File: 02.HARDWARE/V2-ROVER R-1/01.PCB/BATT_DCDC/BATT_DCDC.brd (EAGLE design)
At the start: 20.4 x 34.4 mm, 61 parts, among them J1 DF40C-20DP-0.4V_51_, K1 FLEX11, Q1 NVTFS9D6P04M8LTAG, Q2 2N7002PW, Q5 2N7002PW, U1 MCP6071T-E/OT, U3 TPS55330RTET, U7 MCP6071T-E/OT

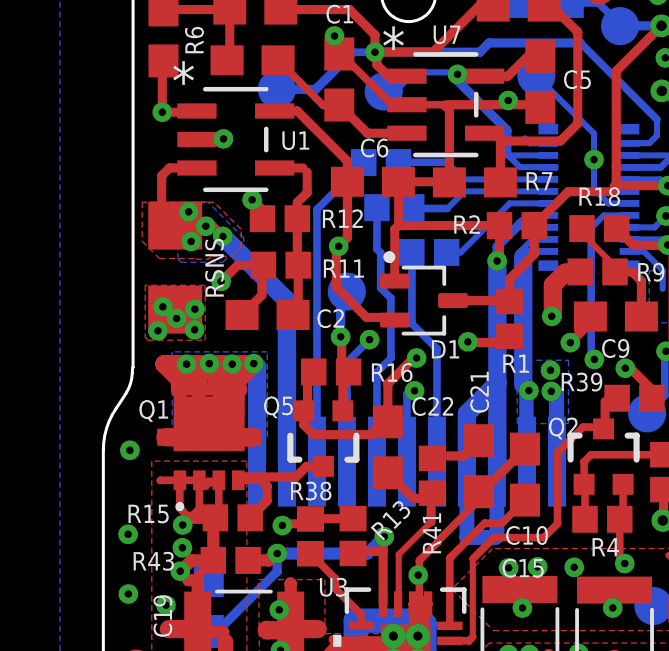
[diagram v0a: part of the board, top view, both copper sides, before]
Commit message: Separacion de las vias de la zona de cobre descubierto en la resistencia de sensado
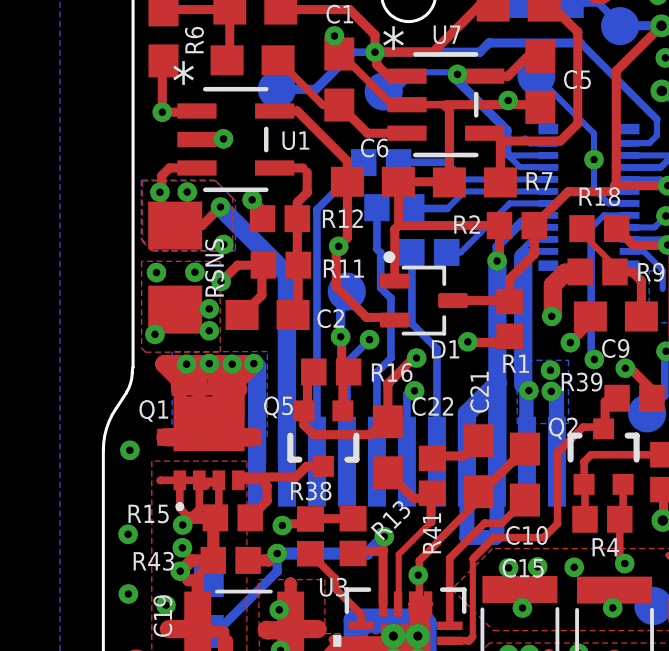
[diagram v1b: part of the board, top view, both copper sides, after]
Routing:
- net ISENSE_RAW: track 13.7 -> 16.4 mm
- net VOUT-: track 13.3 -> 14.3 mm

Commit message: Cierra el issue #65
Algunos cambios menores de rutado
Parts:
- moved R9 0.33 mm to (73.7, 25.9)
- moved R2 0.07 mm to (71.3, 27.4)
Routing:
- net VBUS: track 56.4 -> 64.9 mm
- net N$12: track 4.09 -> 4.95 mm
- net GND: vias 45 -> 46
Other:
- board text added: "BATT_DCDC ROVER R-1 v3-MAY'23"
- board text removed: "BATT_DCDC ROVER1K v2-DEC'22"

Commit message: Issue #72
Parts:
- removed Q5: 2N7002PW, SparkFun-DiscreteSemi:SOT323
- removed R15: 100k, SparkFun-Resistors:0402
- added U2: LM5114BMF_NOPB, LM5114BMF_NOPB:SOT95P280X145-6N
- R16: value 100k -> 10k
- moved C22 3.39 mm to (69.7, 22.0), turned to 180 degrees
- moved R16 0.78 mm to (65.9, 22.7), turned to 0 degrees
- moved C21 0.29 mm to (70.2, 19.2), turned to 270 degrees
- moved R41 0.29 mm to (68.8, 19.0), turned to 270 degrees
- moved C10 0.26 mm to (71.8, 19.1)
- moved R13 0.16 mm to (65.8, 16.9)
- moved R38 0.13 mm to (64.4, 16.9)
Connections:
- removed net N$8: Q1.4, Q5.3, R15.1
- new net N$9: Q1.4, U2.2, U2.3
- net GND: now also U2.4; no longer Q5.2
- net OP_SWITCH: now also U2.5; no longer Q5.1
- net VSOURCE: now also U2.1; no longer R15.2
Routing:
- net N$9: track 0.00 -> 5.95 mm
- net N$8: track 5.44 -> 0.00 mm
- net VSOURCE: track 34.7 -> 37.4 mm
- net COMP_TPS: track 6.07 -> 8.37 mm
- net SW2_TPS: track 29.6 -> 28.0 mm
- net VBUS: track 64.9 -> 63.5 mm
- net GND: track 141.2 -> 140.0 mm, vias 46 -> 47
- net OP_SWITCH: track 28.8 -> 28.1 mm
- net N$35: track 5.56 -> 6.13 mm
- net VOUT+: track 32.5 -> 33.0 mm
- net N$2: track 9.35 -> 9.85 mm

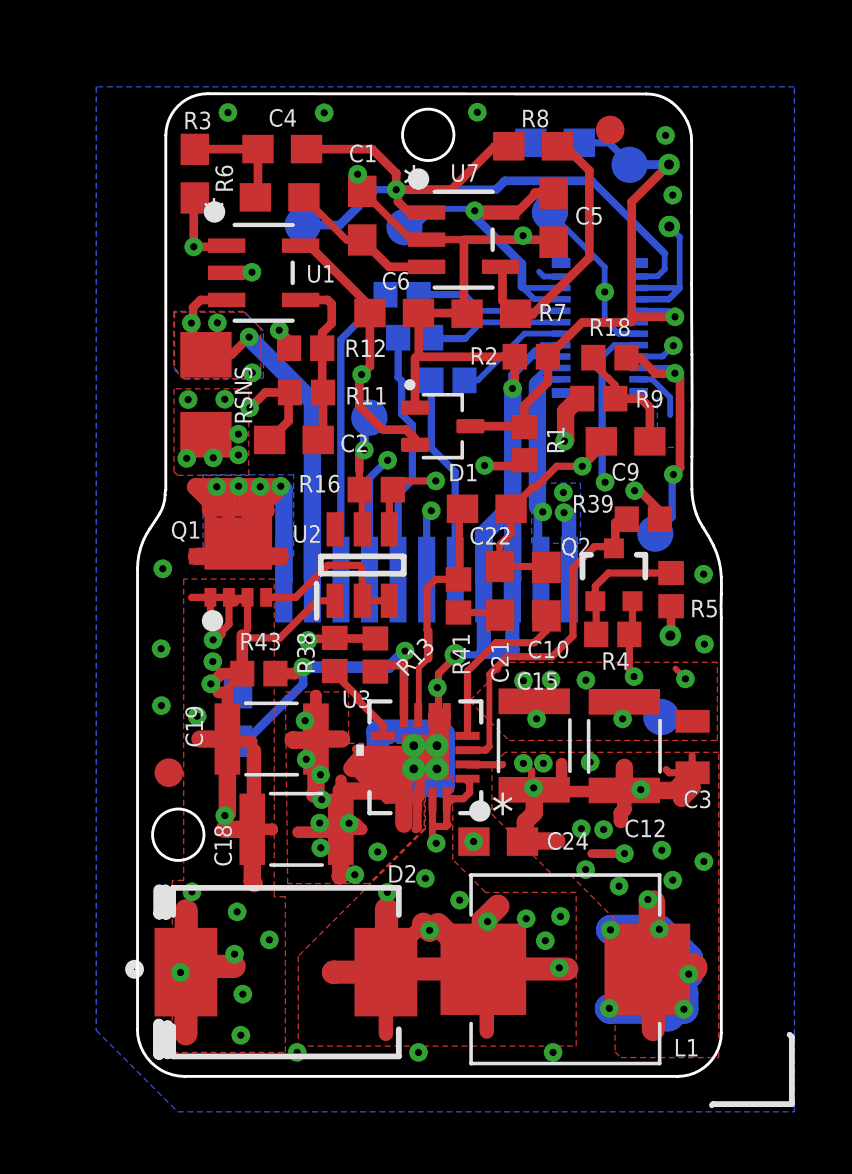
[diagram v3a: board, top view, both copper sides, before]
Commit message: Se corrige señal IN a VSOURCE para  que funcione como negador
Se mueven algunos componentes para  que no se solapen.
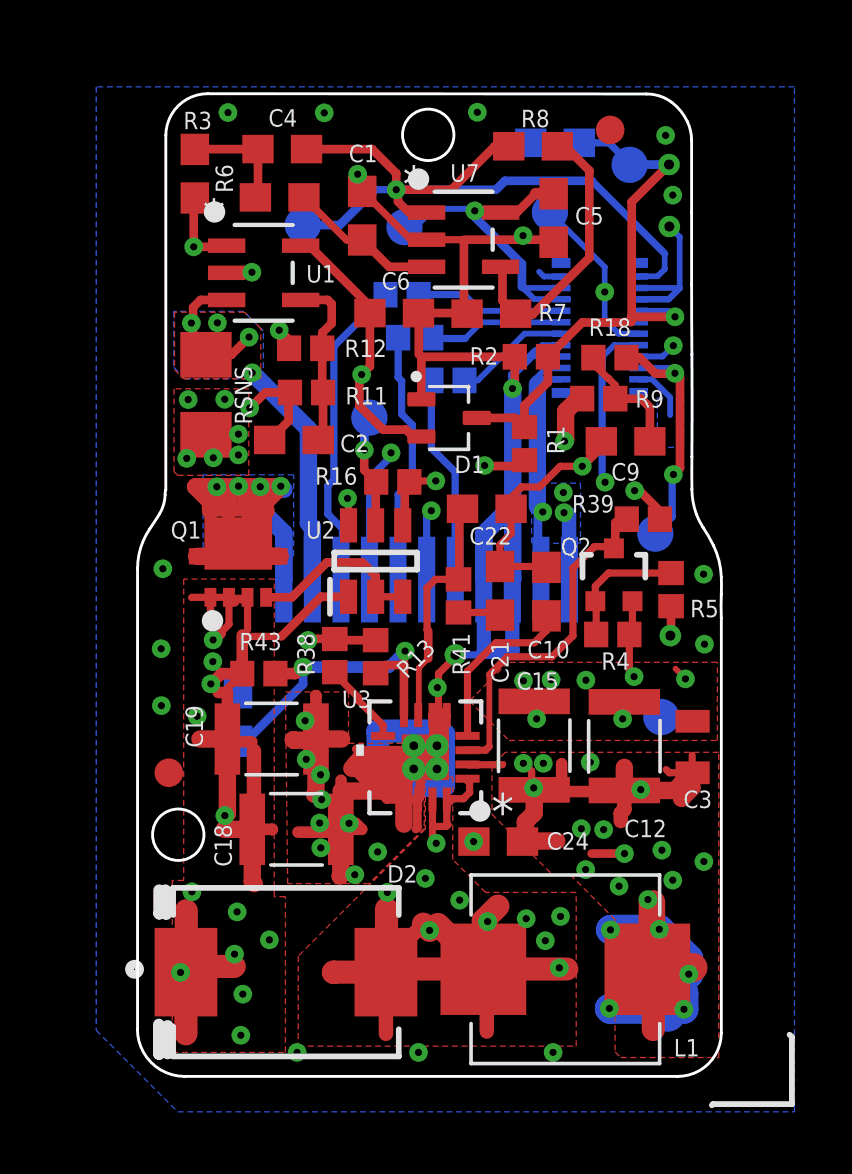
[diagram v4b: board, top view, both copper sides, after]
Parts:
- moved R16 0.64 mm to (66.5, 23.0)
- moved U2 0.49 mm to (65.8, 20.2)
- moved D1 0.36 mm to (68.4, 25.2)
- moved R13 0.06 mm to (65.8, 16.9)
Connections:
- net VSOURCE: now also U2.6
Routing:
- net VSOURCE: track 37.4 -> 45.8 mm, vias 12 -> 13
- net VOUT-: track 14.3 -> 13.1 mm
- net GND: track 140.0 -> 139.3 mm
- net VCC: track 49.0 -> 48.5 mm
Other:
- board text added: "BATT_DCDC ROVER R-1 v4-SEP'23"
- board text removed: "BATT_DCDC ROVER R-1 v3-MAY'23"

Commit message: Revision antes de envio SETI 3ra produccion - SEP-23
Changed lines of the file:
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@@
 <drawing>
 <settings>
-<setting alwaysvectorfont="no"/>
+<setting alwaysvectorfont="yes"/>
 <setting keepoldvectorfont="yes"/>
 <setting verticaltext="up"/>
@@
 <layer number="14" name="Route14" color="1" fill="6" visible="no" active="no"/>
 <layer number="15" name="Route15" color="13" fill="1" visible="no" active="yes"/>
-<layer number="16" name="Bottom" color="1" fill="1" visible="no" active="yes"/>
+<layer number="16" name="Bottom" color="1" fill="1" visible="yes" active="yes"/>
 <layer number="17" name="Pads" color="2" fill="1" visible="yes" active="yes"/>
 <layer number="18" name="Vias" color="2" fill="1" visible="yes" active="yes"/>
 <layer number="19" name="Unrouted" color="6" fill="1" visible="yes" active="yes"/>
 <layer number="20" name="Dimension" color="15" fill="1" visible="yes" active="yes"/>
-<layer number="21" name="tPlace" color="14" fill="1" visible="no" active="yes"/>
+<layer number="21" name="tPlace" color="14" fill="1" visible="yes" active="yes"/>
 <layer number="22" name="bPlace" color="13" fill="1" visible="yes" active="yes"/>
 <layer number="23" name="tOrigins" color="14" fill="1" visible="no" active="yes"/>
 <layer number="24" name="bOrigins" color="13" fill="1" visible="yes" active="yes"/>
-<layer number="25" name="tNames" color="7" fill="1" visible="no" active="yes"/>
+<layer number="25" name="tNames" color="7" fill="1" visible="yes" active="yes"/>
 <layer number="26" name="bNames" color="7" fill="1" visible="yes" active="yes"/>
 <layer number="27" name="tValues" color="7" fill="1" visible="no" active="yes"/>
@@
 <circle x="67.35" y="33.57" radius="0.17204375" width="0.4064" layer="21"/>
 <rectangle x1="59.8" y1="21.36" x2="62.28" y2="22.62" layer="29"/>
+<circle x="63.76" y="18.94" radius="0.17204375" width="0.4064" layer="21"/>
 </plain>
 <attributes>
@@
 </element>
 <element name="Q2" library="SparkFun-DiscreteSemi" package="SOT323" value="2N7002PW" x="74.19" y="19.72" smashed="yes">
-<attribute name="NAME" x="72.8645" y="20.708" size="0.6096" layer="25" font="vector" align="center"/>
+<attribute name="NAME" x="72.9345" y="21.028" size="0.6096" layer="25" font="vector" align="center"/>
 <attribute name="PROD_ID" value="TRANS-11151" x="1.11" y="5.46" size="1.778" layer="27" display="off"/>
 </element>
@@
 </element>
 <element name="R1" library="SparkFun-Resistors" library_urn="urn:adsk.eagle:library:532" package="0402" package3d_urn="urn:adsk.eagle:package:39657/1" value="169k" x="71.06" y="24.31" smashed="yes" rot="R90">
-<attribute name="NAME" x="72.152" y="24.44" size="0.6096" layer="25" font="vector" rot="R270" align="center"/>
+<attribute name="NAME" x="70.002" y="24.5" size="0.6096" layer="25" font="vector" rot="R270" align="center"/>
 <attribute name="PROD_ID" value=" " x="67.51" y="24.91" size="1.778" layer="27" rot="R90" display="off"/>
 <attribute name="VALUE" x="71.822" y="24.31" size="0.6096" layer="27" font="vector" ratio="20" rot="R90" align="top-center"/>
@@
 <attribute name="MF" value="Nexperia USA Inc." x="68.42" y="25.21" size="1.778" layer="27" display="off"/>
 <attribute name="MP" value="BAT54SW,115" x="68.42" y="25.21" size="1.778" layer="27" display="off"/>
-<attribute name="NAME" x="68.609290625" y="23.280709375" size="0.6096" layer="25" font="vector"/>
+<attribute name="NAME" x="68.099290625" y="23.220709375" size="0.6096" layer="25" font="vector"/>
 <attribute name="PACKAGE" value="SOT-323 Nexperia USA Inc." x="68.42" y="25.21" size="1.778" layer="27" display="off"/>
 <attribute name="PRICE" value="None" x="68.42" y="25.21" size="1.778" layer="27" display="off"/>
@@
 <wire x1="65.8882" y1="15.0318" x2="65.8882" y2="12.92" width="1.27" layer="2"/>
 <wire x1="68.01" y1="15.0318" x2="65.8882" y2="15.0318" width="1.27" layer="2"/>
-<wire x1="68.01" y1="15.77" x2="68.01" y2="13.01" width="1.27" layer="2"/>
-<wire x1="68.01" y1="13.01" x2="68" y2="13" width="1.27" layer="2"/>
+<wire x1="68.01" y1="15.77" x2="67.63" y2="15.39" width="1.27" layer="2"/>
+<wire x1="67.63" y1="15.39" x2="67.63" y2="13.02" width="1.27" layer="2"/>
 <wire x1="71.99" y1="31.45" x2="72.08" y2="31.36" width="0.3048" layer="1"/>
 <wire x1="68.94" y1="31.45" x2="71.99" y2="31.45" width="0.3048" layer="1"/>
@@
 <wire x1="59.21" y1="5.81" x2="59.37" y2="5.97" width="0.508" layer="1"/>
 <wire x1="60.715" y1="18.87" x2="61.33" y2="18.87" width="0.3048" layer="1"/>
-<polygon width="0.3048" layer="1">
+<polygon width="0.2" layer="1" isolate="0.254" rank="2">
 <vertex x="62.69" y="8.45"/>
 <vertex x="62.3" y="8.45"/>
@@
 <contactref element="U7" pad="5"/>
 <contactref element="R39" pad="1"/>
-<wire x1="64.705" y1="23.365" x2="64.705" y2="26.265" width="0.3048" layer="2"/>
+<wire x1="64.705" y1="23.725" x2="64.705" y2="26.265" width="0.3048" layer="2"/>
 <via x="65.36" y="26.73" extent="1-16" drill="0.25"/>
 <wire x1="66.11" y1="24.8" x2="65.28" y2="25.63" width="0.3048" layer="1"/>
@@
 <wire x1="75.8" y1="21.95" x2="75.8" y2="21.665" width="0.2032" layer="1"/>
 <via x="74.915" y="22.665" extent="1-16" drill="0.25"/>
-<wire x1="65.09" y1="22.98" x2="64.705" y2="23.365" width="0.3048" layer="2"/>
+<wire x1="65.29" y1="23.14" x2="64.705" y2="23.725" width="0.3048" layer="2"/>
 <contactref element="C5" pad="1"/>
 <contactref element="C6" pad="1"/>
@@
 <wire x1="74.915" y1="22.665" x2="74.895" y2="22.685" width="0.2032" layer="2"/>
 <wire x1="74.895" y1="23.655" x2="73.44" y2="25.11" width="0.3048" layer="2"/>
-<wire x1="65.09" y1="22.98" x2="66.79" y2="22.98" width="0.3048" layer="2"/>
+<wire x1="65.29" y1="23.14" x2="66.95" y2="23.14" width="0.3048" layer="2"/>
 <wire x1="68.92" y1="25.11" x2="73.44" y2="25.11" width="0.3048" layer="2"/>
 <via x="69.32" y="32.46" extent="1-16" drill="0.25"/>
@@
 <wire x1="71.07" y1="29.76" x2="71.04" y2="29.73" width="0.2032" layer="16"/>
 <wire x1="71.4002" y1="29.3698" x2="72.59" y2="29.3698" width="0.2032" layer="16"/>
-<wire x1="66.79" y1="22.98" x2="68.92" y2="25.11" width="0.3048" layer="2"/>
+<wire x1="66.95" y1="23.14" x2="68.92" y2="25.11" width="0.3048" layer="2"/>
 <wire x1="72.59" y1="29.3698" x2="72.345" y2="29.36" width="0" layer="19" extent="16-16"/>
 </signal>

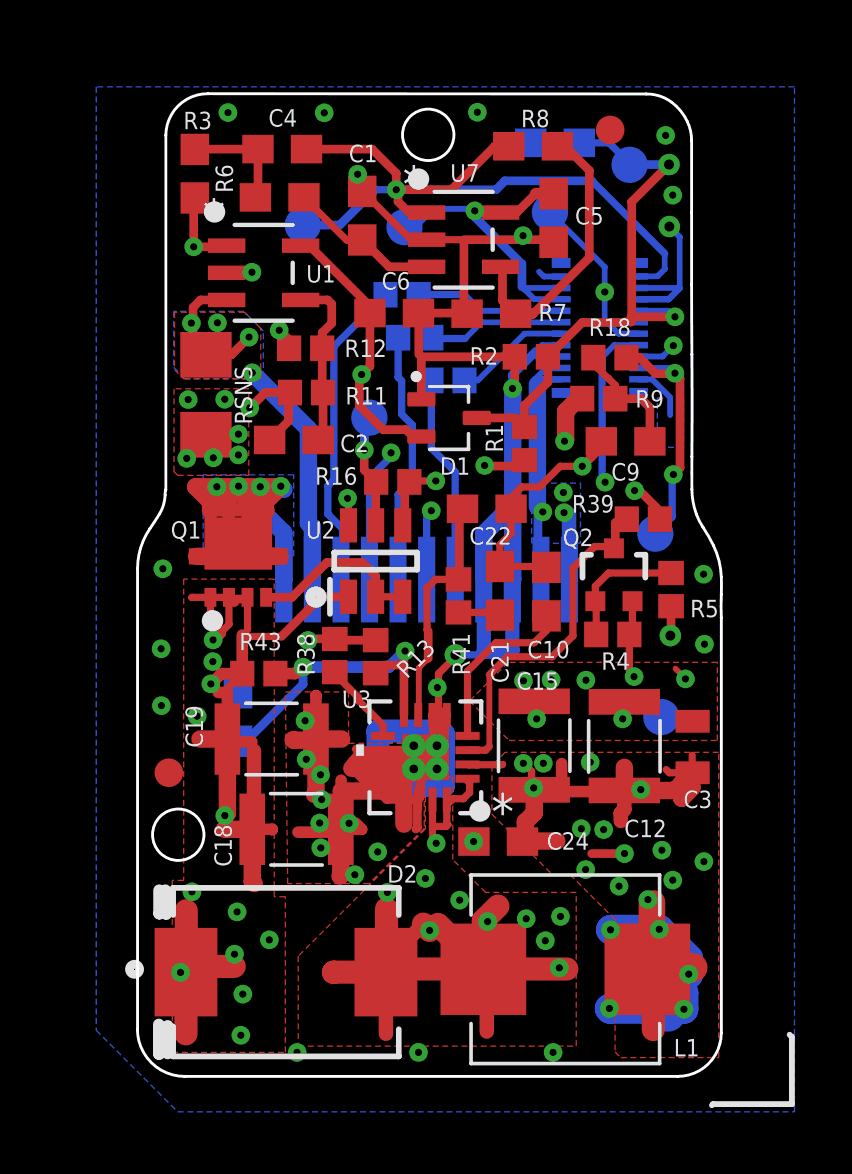
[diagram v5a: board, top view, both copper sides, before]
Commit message: Modificacion DCDC y Conector
DCDC: Posible version exclusiva PMU
Conector: Adatacion a cambio en produccion de un componente (SMJ)
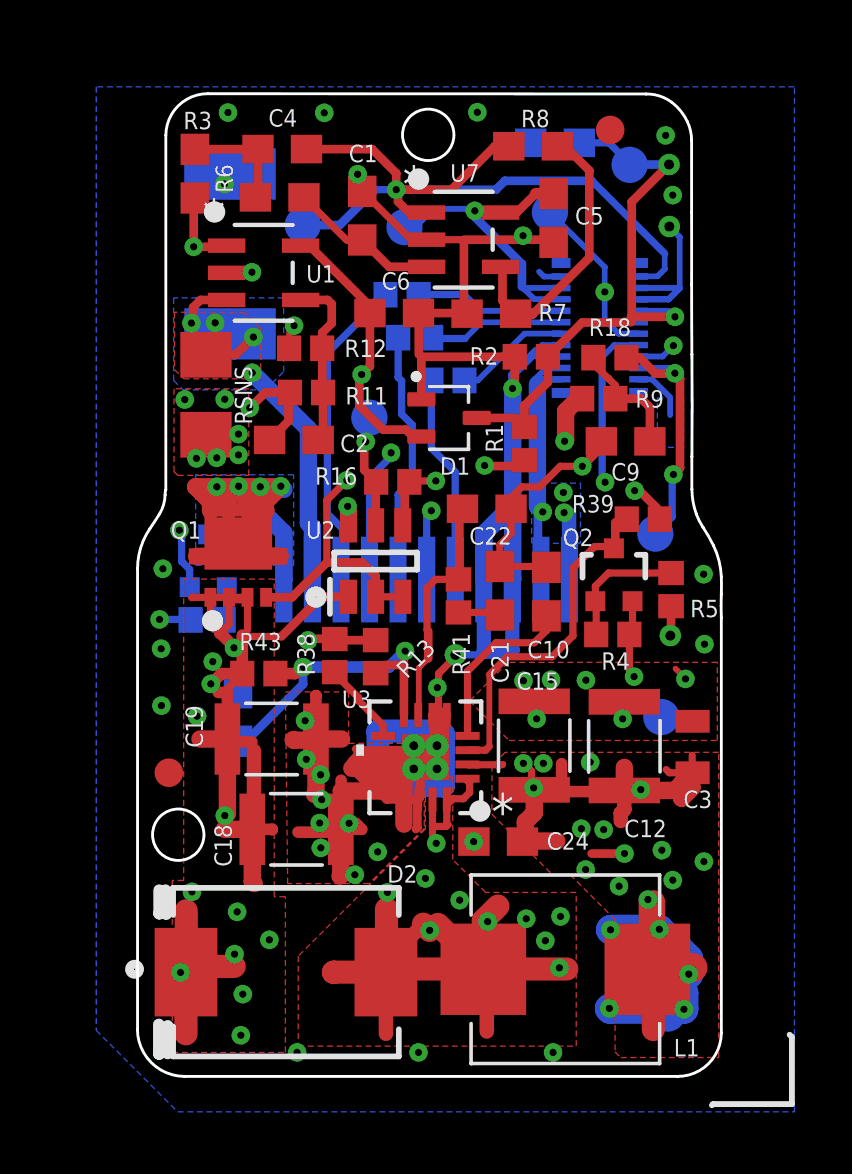
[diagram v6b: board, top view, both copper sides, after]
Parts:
- added Q3: 2N7002PW, SparkFun-DiscreteSemi:SOT323
- added R15: (no value), adafruit:R2512
- added R19: 10k, SparkFun-Resistors:0402
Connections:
- new net N$13: Q3.1, R19.2
- new net N$8: Q3.2, R15.2
- net N$9: now also R19.1
- net VOUT+: now also Q3.3
- net VOUT-: now also R15.1
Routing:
- net N$8: track 0.00 -> 15.7 mm, vias 0 -> 2
- net N$9: track 6.22 -> 19.0 mm, vias 0 -> 2
- net N$13: track 0.00 -> 1.19 mm

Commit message: Correccion errores e inclusion Fiducial Marks en DCDC
Se divide en 2 la RBalastro.
Recolocación a parte superior.
Inclusión 2 fiduciales en la parte del botom
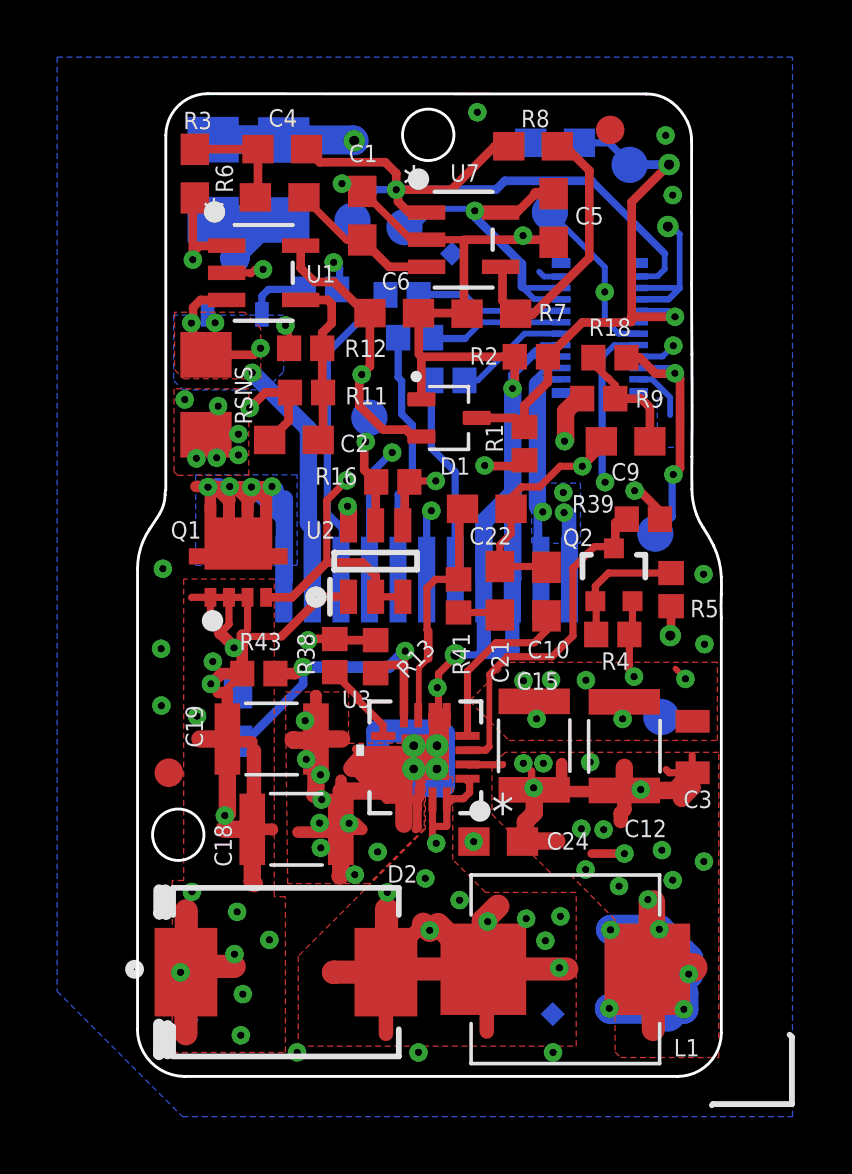
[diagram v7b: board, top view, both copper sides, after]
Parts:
- added FD_1, FD_2, FD_3: FD_1, testpad:TP06SQ
- added R20: 20R, SparkFun-Resistors:1206
- Q3: value 2N7002PW -> PMV20XNER; device SparkFun-DiscreteSemi:SOT323 -> PMV20XNER:SOT23-TO-236AB_NEX-L
- R15: value (none) -> 20R; device adafruit:R2512 -> SparkFun-Resistors:1206
- R19: value 10k -> 33R
- moved R19 12.2 mm to (63.9, 29.7), turned to 0 degrees
- moved Q3 9.63 mm to (60.9, 29.8)
- moved R15 3.20 mm to (62.6, 33.5)
- moved IOSENSE 1.75 mm to (65.0, 32.1)
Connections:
- net N$8: now also Q3.3, R15.1, R20.1; no longer Q3.2, R15.2
- net VOUT+: now also R15.2, R20.2; no longer Q3.3
- net VOUT-: now also Q3.2; no longer R15.1
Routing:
- net VOUT+: track 33.5 -> 52.3 mm, vias 5 -> 6
- net N$8: track 15.7 -> 6.57 mm, vias 2 -> 0
- net IOSENSE: track 26.2 -> 24.5 mm
- net ISENSE_RAW: track 16.8 -> 15.4 mm
- net N$13: track 1.19 -> 2.21 mm
- net GND: track 139.6 -> 140.6 mm, vias 47 -> 45
- net VSOURCE: track 45.9 -> 45.0 mm
- net N$9: track 19.0 -> 18.4 mm
